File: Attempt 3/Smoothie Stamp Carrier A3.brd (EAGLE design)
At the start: 150 x 100 mm, 33 parts

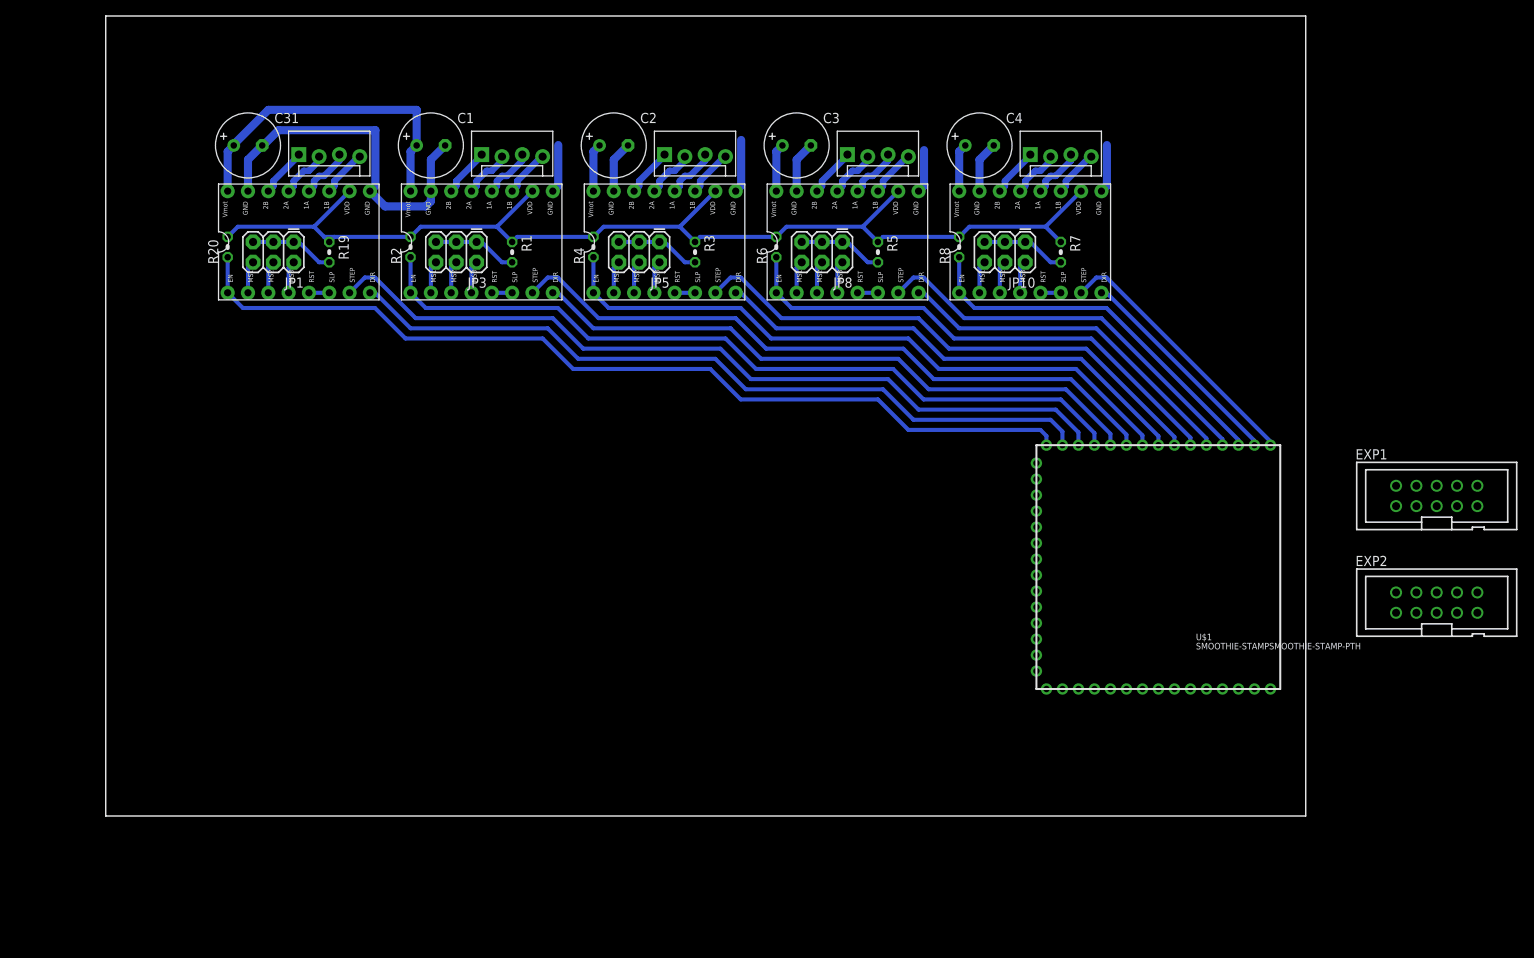
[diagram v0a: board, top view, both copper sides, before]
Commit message: Motors consolidated, 4 mosfets placed, first glcd attempt
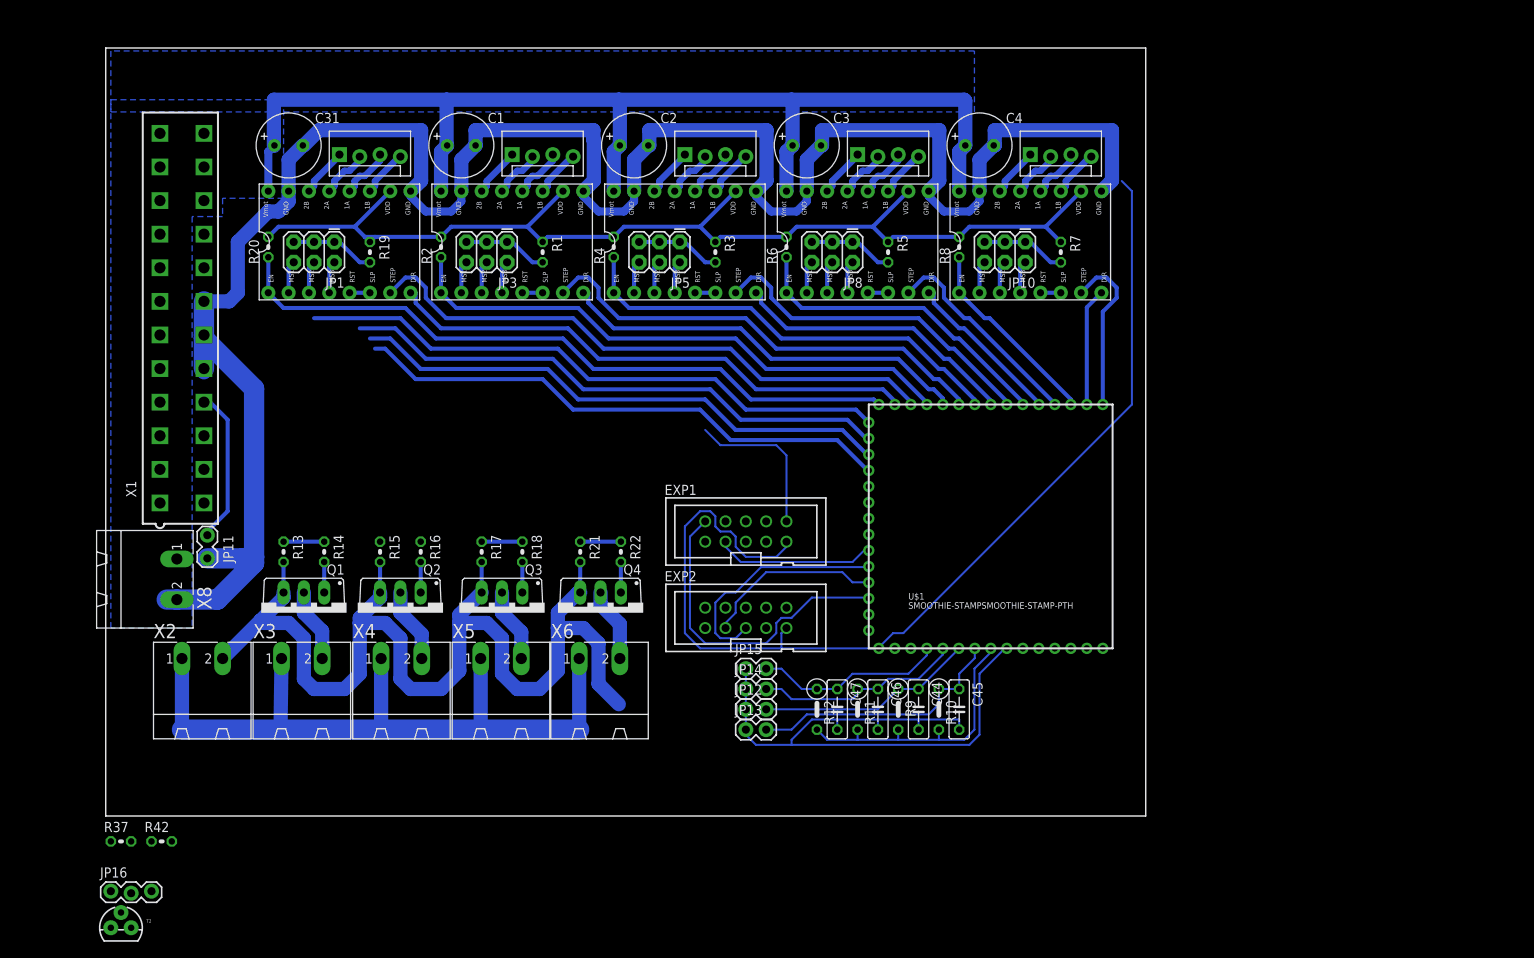
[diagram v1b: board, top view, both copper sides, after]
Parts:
- added C44, C45, C46, C47: 10uF, rcl:C050-025X075
- added JP11: (no value), SparkFun-Connectors:1X02_LOCK
- added JP12, JP13, JP14, JP15: (no value), SparkFun-Connectors:1X02
- added JP16: (no value), SparkFun-Connectors:1X03_LOCK
- added Q1, Q2, Q3, Q4: STP55NF06L, transistor-power:TO220BV
- added R10, R11, R12, R9: 4.7k, rcl:0207/5V
- added R13, R15, R17, R21, R42: 100k, rcl:0204V
- added R14, R16, R18, R22, R37: 10r, rcl:0204V
- added T2: BC817, SparkFun-DiscreteSemi:TO-92
- added X1: 5566-24, con-molex:5566-24
- added X2, X3, X4, X5, X6, X8: MSTBA2, con-phoenix-508:MSTBA2
- moved EXP1 86.5 mm to (80.0, 35.6)
- moved EXP2 86.4 mm to (80.0, 24.8)
- moved U$1 21.6 mm to (95.2, 21.0)
- moved JP6 5.08 mm to (29.2, 82.5)
- moved R19 5.08 mm to (33.0, 70.5)
- moved R20 5.08 mm to (20.3, 71.1)
- moved C31 5.08 mm to (22.9, 83.8)
- moved JP1 5.08 mm to (28.6, 71.8)
- moved U$2 5.08 mm to (21.6, 76.8)
- moved C1 3.81 mm to (44.5, 83.8)
- moved JP3 3.81 mm to (50.2, 71.8)
- moved R1 3.81 mm to (54.6, 70.5)
- moved U$3 3.81 mm to (43.2, 76.8)
- moved JP2 3.81 mm to (50.8, 82.5)
- moved R2 3.81 mm to (41.9, 71.1)
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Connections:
- net N$50 renamed P1_22-3RD-SMALL-FET
- net N$51 renamed P1_23-3RD-LARGE-FET
- new net +5V: X1.21
- new net +5VSB: X1.9
- new net 12V: C1.+, C2.+, C3.+, C31.+, C4.+, U$2.VMOT, U$3.VMOT, U$4.VMOT, U$5.VMOT, U$6.VMOT, X1.10, X1.11, X8.1
- new net 12V1: X2.1, X3.1, X4.1, X5.1, X6.1
- new net AGND: C44.2, C45.2, C46.2, C47.2, JP12.1, JP13.1, JP14.1, JP15.1, U$1.AGND
- new net AVCC: R10.2, R11.2, R12.2, R9.2, U$1.AVCC
- new net N$50: Q3.D, X5.2
- new net N$51: Q4.G, R22.2
- new net N$52: U$1.X_MIN
- new net N$53: U$1.X_MAX
- new net N$54: U$1.Y_MIN
- new net N$55: U$1.Y_MAX
- new net N$56: U$1.Z_MIN
- new net N$57: U$1.Z_MAX
- new net N$58: Q4.D, X6.2
- new net N$59: Q1.G, R14.2
- new net N$60: JP16.2, T2.3
- new net N$61: R37.2, R42.2, T2.2
- new net N$64: U$1.RX_0
- new net N$65: U$1.TX_0
- new net P2.6_FAN_FET: R15.1, R16.1, R37.1, U$1.P2.6_FAN_FET
- new net P2.7_HOTEND_FET: R13.1, R14.1, U$1.P2.7_HOTEND_FET
- new net PSUON: JP11.2, X1.16
- new net PWM0_PSU_OUT: R21.1, R22.1, U$1.PWM0_PSU_OUT
- new net PWM1_BED_HEATER: R17.1, R18.1, U$1.PWM1_BED_HEATER
- new net TH1_HOTEND: C45.1, JP13.2, R10.1, U$1.TH1_HOTEND
- new net TH2_BED: C44.1, JP12.2, R9.1, U$1.TH2_BED
- new net TH3: C46.1, JP14.2, R11.1, U$1.TH3
- new net TH4: C47.1, JP15.2, R12.1, U$1.TH4
- net 24V: now also JP16.1; no longer C1.+, C2.+, C3.+, C31.+, C4.+, U$2.VMOT, U$3.VMOT, U$4.VMOT, U$5.VMOT, U$6.VMOT
- net 5V: now also JP16.3
- net GND: now also JP11.1, Q1.S, Q2.S, Q3.S, Q4.S, R13.2, R15.2, R17.2, R21.2, R42.1, T2.1, X1.17, X1.18, X1.19, X2.2, X8.2
- net N$46: now also Q1.D, X3.2; no longer U$1.P2.7_HOTEND_FET
- net N$47: now also Q2.G, R16.2; no longer U$1.PWM1_BED_HEATER
- net N$48: now also Q2.D, X4.2; no longer U$1.P2.6_FAN_FET
- net N$49: now also Q3.G, R18.2; no longer U$1.PWM0_PSU_OUT
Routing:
- net GND: track 89.2 -> 546.8 mm
- net 12V: track 0.00 -> 145.3 mm
- net 12V1: track 0.00 -> 94.1 mm
- net P2.7_HOTEND_FET: track 0.00 -> 79.8 mm
- net AGND: track 0.00 -> 78.6 mm
- net PWM1_BED_HEATER: track 0.00 -> 73.5 mm
- net PWM0_PSU_OUT: track 0.00 -> 73.1 mm
- net P2.6_FAN_FET: track 0.00 -> 69.5 mm
- net 24V: track 59.4 -> 0.00 mm
- net P1_30_CLICK-ON-RRD: track 0.00 -> 40.4 mm
- net AVCC: track 0.00 -> 36.3 mm
- net TH1_HOTEND: track 0.00 -> 33.2 mm
- net SD_IRQ-ENC-A-ON-RRD: track 0.00 -> 29.4 mm
- net EN1: track 115.4 -> 86.5 mm
- net STP1: track 101.5 -> 73.4 mm
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- added copper zone on layer 16, net 12V
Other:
- board size 150 x 100 mm -> 130 x 96 mm

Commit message: Dedicated Power In for Bed MOSFET, rev1 board don
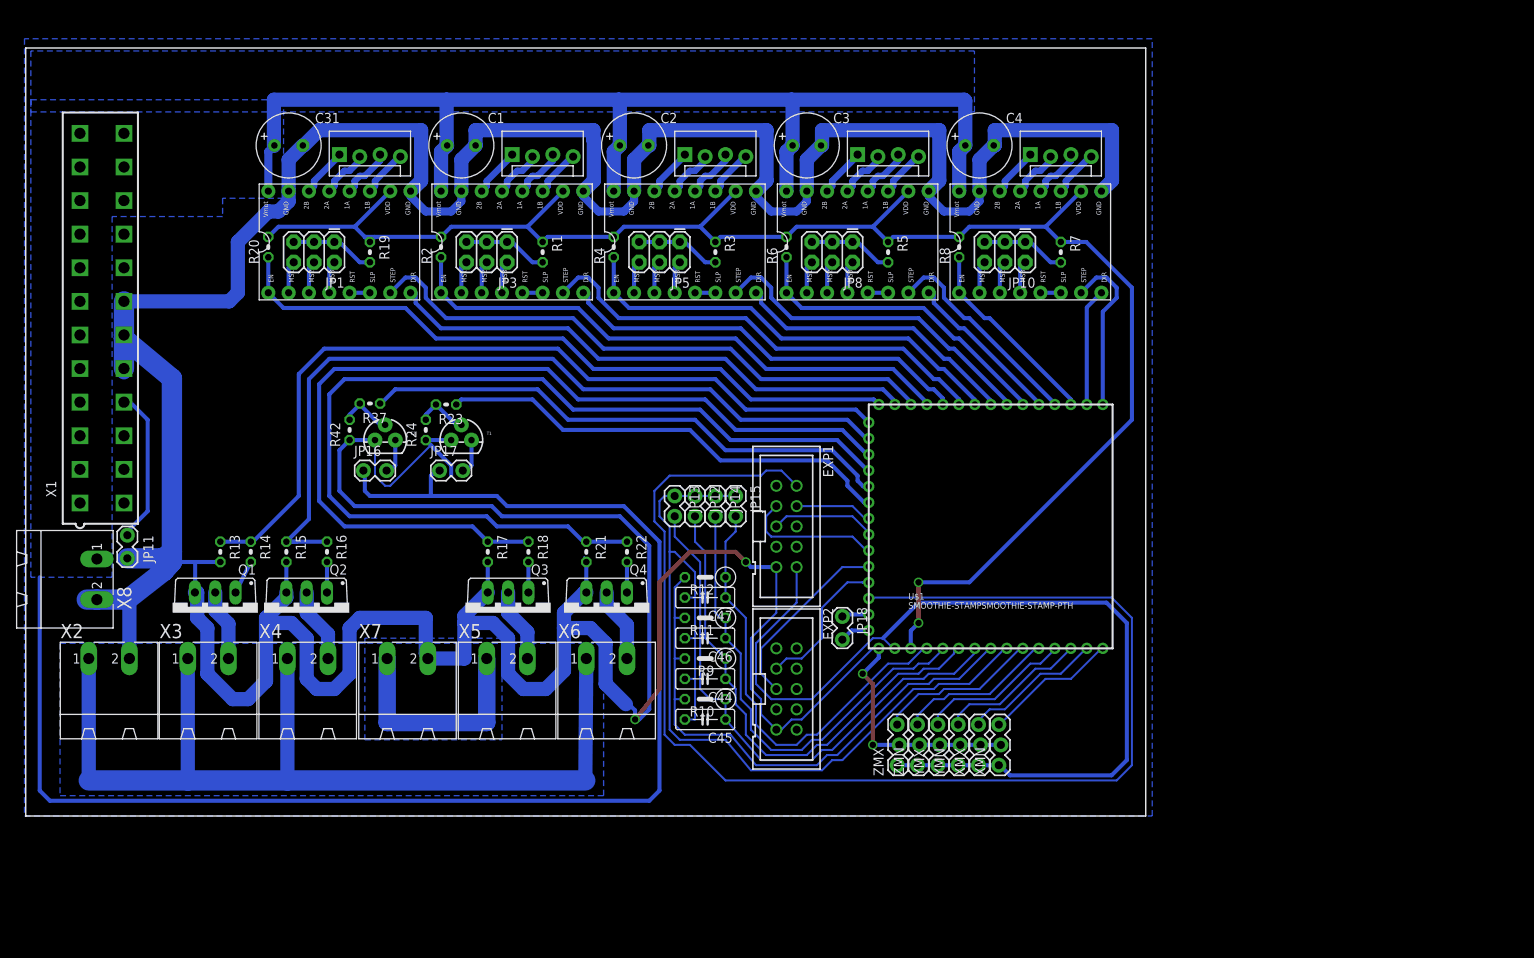
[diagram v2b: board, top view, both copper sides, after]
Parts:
- added JP17, JP18: (no value), SparkFun-Connectors:1X02_LOCK
- added R23: 10r, rcl:0204V
- added R24: 100k, rcl:0204V
- added T1: BC817, SparkFun-DiscreteSemi:TO-92
- added X7: MSTBA2, con-phoenix-508:MSTBA2
- added XMN, XMX, YMN, YMX, ZMN, ZMX: (no value), SparkFun-Connectors:1X03_LOCK
- JP16: device SparkFun-Connectors:1X03_LOCK -> SparkFun-Connectors:1X02_LOCK
- moved T2 69.3 mm to (34.9, 47.0)
- moved R37 63.0 mm to (33.0, 51.6), turned to 180 degrees
- moved JP16 61.5 mm to (32.4, 43.2)
- moved R42 56.5 mm to (30.5, 48.3), turned to 90 degrees
- moved C45 31.8 mm to (74.9, 12.1), turned to 180 degrees
- moved JP13 30.5 mm to (71.1, 40.0), turned to 270 degrees
- moved R10 29.2 mm to (74.9, 14.6), turned to 180 degrees
- moved JP12 27.4 mm to (73.7, 40.0), turned to 270 degrees
- moved C44 26.9 mm to (74.9, 17.1), turned to 180 degrees
- moved R9 25.0 mm to (74.9, 19.7), turned to 180 degrees
- moved JP14 24.4 mm to (76.2, 40.0), turned to 270 degrees
- moved C46 23.3 mm to (74.9, 22.2), turned to 180 degrees
- moved R11 22.2 mm to (74.9, 24.8), turned to 180 degrees
- moved JP15 21.6 mm to (78.7, 40.0), turned to 270 degrees
- moved R12 21.6 mm to (74.9, 29.8), turned to 180 degrees
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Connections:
- removed net 24V: JP16.1
- removed net N$52: U$1.X_MIN
- removed net N$53: U$1.X_MAX
- removed net N$54: U$1.Y_MIN
- removed net N$55: U$1.Y_MAX
- removed net N$56: U$1.Z_MIN
- removed net N$57: U$1.Z_MAX
- removed net N$64: U$1.RX_0
- removed net N$65: U$1.TX_0
- new net 12V2: X5.1, X7.1
- new net N$62: JP17.2, T1.3
- new net N$63: R23.2, R24.2, T1.2
- new net RX_0: JP18.2, U$1.RX_0
- new net TX_0: JP18.1, U$1.TX_0
- new net X_MAX: U$1.X_MAX, XMX.3
- new net X_MIN: U$1.X_MIN, XMN.3
- new net Y_MAX: U$1.Y_MAX, YMX.3
- new net Y_MIN: U$1.Y_MIN, YMN.3
- new net Z_MAX: U$1.Z_MAX, ZMX.3
- new net Z_MIN: U$1.Z_MIN, ZMN.3
- net 12V: now also JP16.1, JP17.1
- net 12V1: no longer X5.1
- net 5V: now also XMN.1, XMX.1, YMN.1, YMX.1, ZMN.1, ZMX.1; no longer JP16.3
- net GND: now also R24.1, T1.1, X7.2, XMN.2, XMX.2, YMN.2, YMX.2, ZMN.2, ZMX.2
- net P1_22-3RD-SMALL-FET: now also R23.1
- net P1_23-3RD-LARGE-FET: now also R37.1
- net P2.6_FAN_FET: no longer R37.1
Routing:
- net 12V: track 145.3 -> 327.7 mm
- net P1_30_CLICK-ON-RRD: track 40.4 -> 164.6 mm
- net GND: track 546.8 -> 655.5 mm, vias 0 -> 4
- net 5V: track 19.7 -> 119.1 mm
- net 3.3V: track 139.4 -> 210.9 mm, vias 0 -> 2
- net P1_23-3RD-LARGE-FET: track 0.00 -> 67.4 mm
- net P1_22-3RD-SMALL-FET: track 0.00 -> 57.5 mm
- net PWM0_PSU_OUT: track 73.1 -> 125.5 mm
- net PWM1_BED_HEATER: track 73.5 -> 116.9 mm
- net AGND: track 78.6 -> 117.4 mm
- net TH1_HOTEND: track 33.2 -> 69.6 mm
- net TH2_BED: track 27.3 -> 63.5 mm
- net AVCC: track 36.3 -> 70.6 mm
- net P2.6_FAN_FET: track 69.5 -> 103.2 mm
- net TH3: track 26.1 -> 59.3 mm
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- added copper zone on layer 16, net 12V1
- added copper zone on layer 16, net 12V2
- added copper zone on layer 16, net GND
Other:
- board size 130 x 96 mm -> 140 x 96 mm
